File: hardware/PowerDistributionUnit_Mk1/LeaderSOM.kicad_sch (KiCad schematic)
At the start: 14 parts, among them J10 Logic Analyzer, J11 Logic Analyzer, J12 Logic Analyzer, U1 LeaderSOM

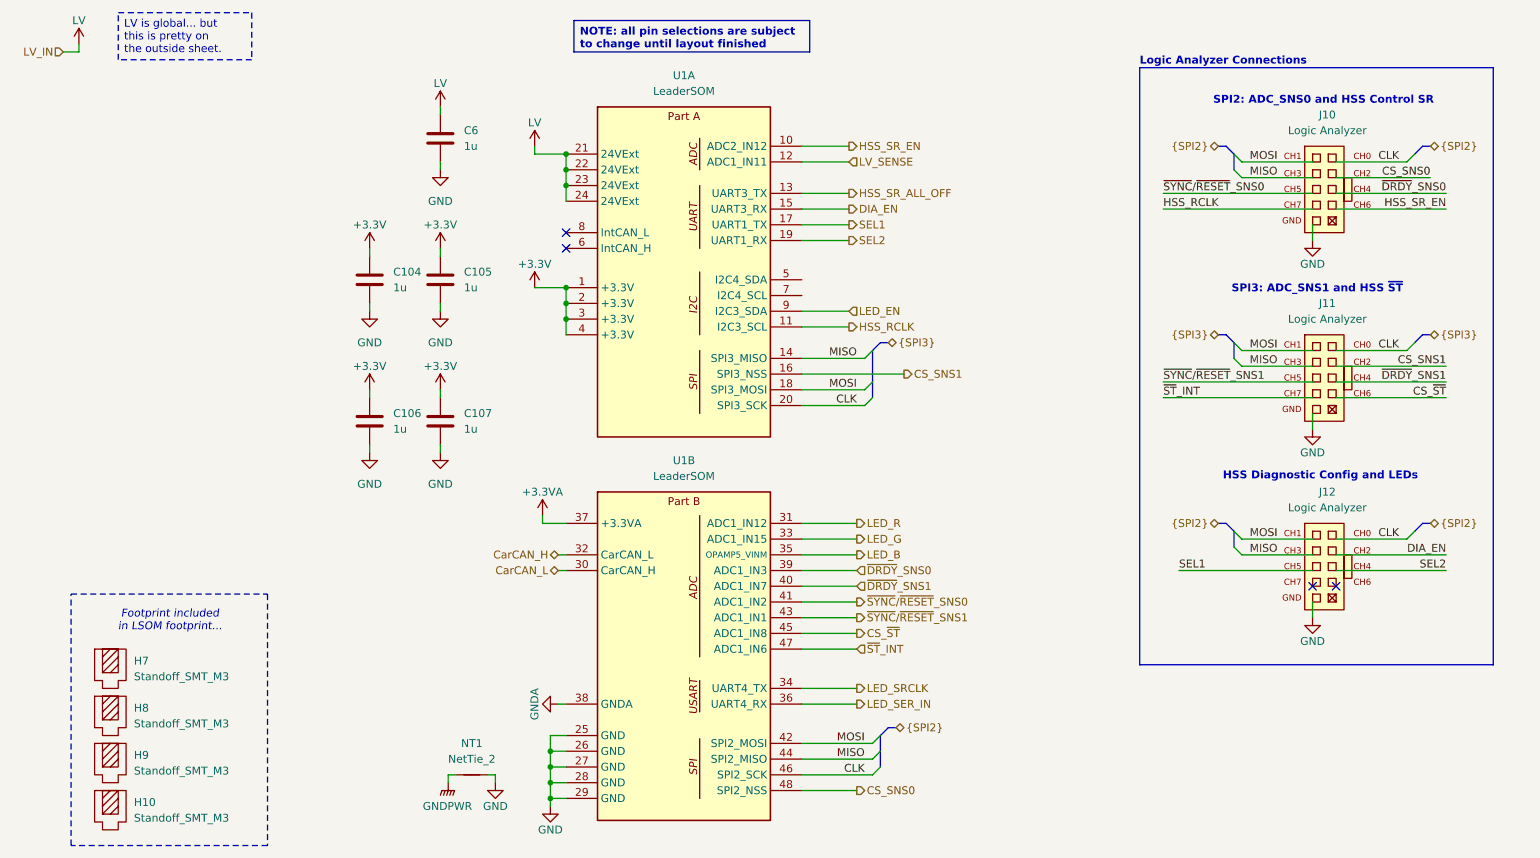
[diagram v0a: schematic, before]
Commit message: schematic updates (found switch, LED resistor values, LV sense ADC pin filter, removed unnecessary parallel resistors, switched to new SR), addressed review comments (input fuse, 3.3V LED, SPI naming fix)
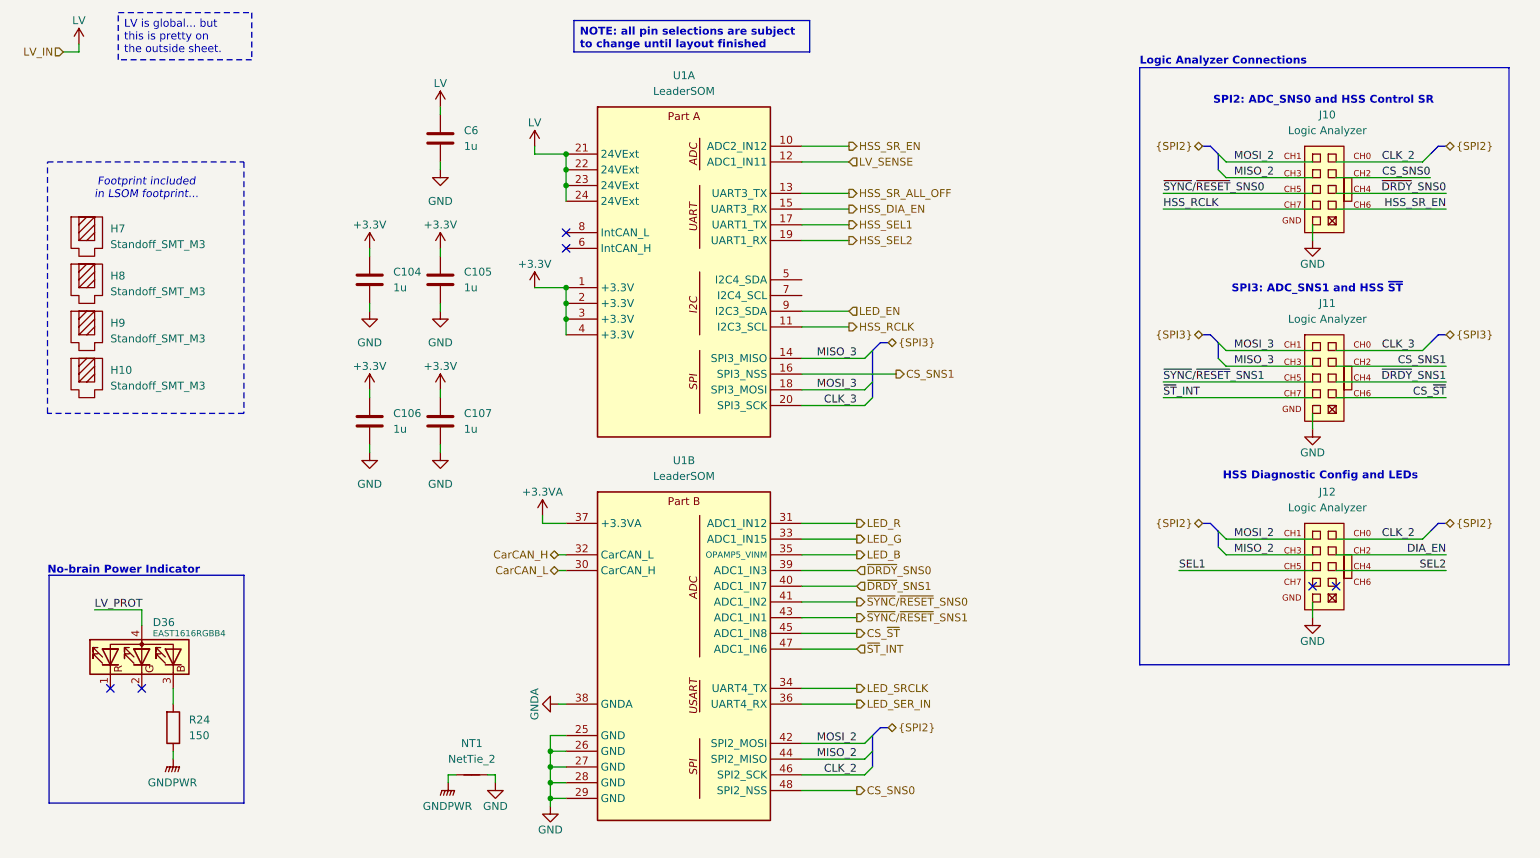
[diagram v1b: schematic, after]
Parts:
- added D36: EAST1616RGBB4, PowerDistributionUnitLib:Everlight_4-SMD, symbol PowerDistributionUnitLib:EAST1616RGBB4
- added R24: 150, Resistor_SMD:R_0603_1608Metric, symbol PowerDistributionUnitResistorLib:150
- U1: footprint PowerDistributionUnitLib:LeaderSOM_Standoff -> UTSVT_Special:LeaderSOM
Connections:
- net DIA_EN: no longer U1.15 (UART3_RX)
- net GNDPWR: now also R24.2
- net SEL1: no longer U1.17 (UART1_TX)
- net SEL2: no longer U1.19 (UART1_RX)
- net CLK renamed CLK_2
- net CLK_2: no longer J11.10 (CH0), U1.20 (SPI3_SCK)
- net MISO renamed MISO_2
- net MISO_2: no longer J11.7 (CH3), U1.14 (SPI3_MISO)
- net MOSI renamed MOSI_2
- net MOSI_2: no longer J11.9 (CH1), U1.18 (SPI3_MOSI)
- new net: D36.3 (BK), R24.1
- new net CLK_3: J11.10 (CH0), U1.20 (SPI3_SCK)
- new net HSS_DIA_EN: U1.15 (UART3_RX)
- new net HSS_SEL1: U1.17 (UART1_TX)
- new net HSS_SEL2: U1.19 (UART1_RX)
- new net LV_PROT: D36.4 (A)
- new net MISO_3: J11.7 (CH3), U1.14 (SPI3_MISO)
- new net MOSI_3: J11.9 (CH1), U1.18 (SPI3_MOSI)
- no-connect marks 4 -> 6
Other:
- note added: "No-brain Power Indicator"
- moved on the sheet: H10, H7, H8, H9

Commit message: fix LeaderSOM footprint, assign proper ADC crystal footprint
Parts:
- U1: footprint UTSVT_Special:LeaderSOM -> PowerDistributionUnitLib:LeaderSOM_Standoff
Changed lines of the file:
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@@
 			)
 		)
-		(property "Footprint" "UTSVT_Special:LeaderSOM"
+		(property "Footprint" "PowerDistributionUnitLib:LeaderSOM_Standoff"
 			(at 138.43 64.77 0)
 			(effects
@@
 			)
 		)
-		(property "Footprint" "UTSVT_Special:LeaderSOM"
+		(property "Footprint" "PowerDistributionUnitLib:LeaderSOM_Standoff"
 			(at 138.43 127 0)
 			(effects

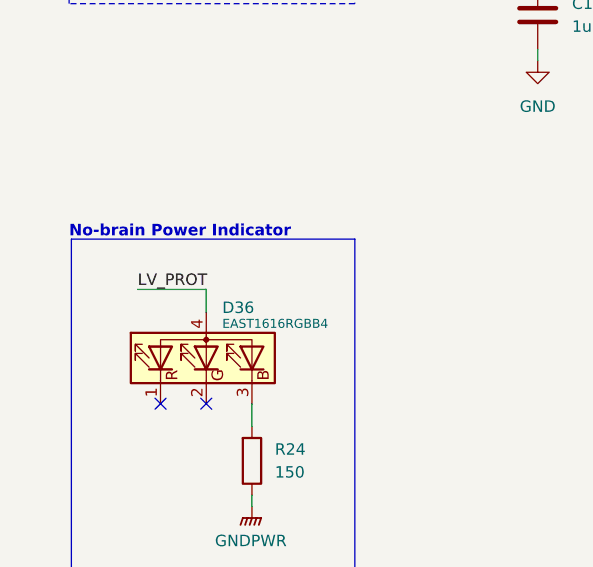
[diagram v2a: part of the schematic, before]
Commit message: started grouping/laying out non HSS components, fixed some schematic things (pins being connected to wrong adjacent thing, LEDs connected to wrong thing, etc.)
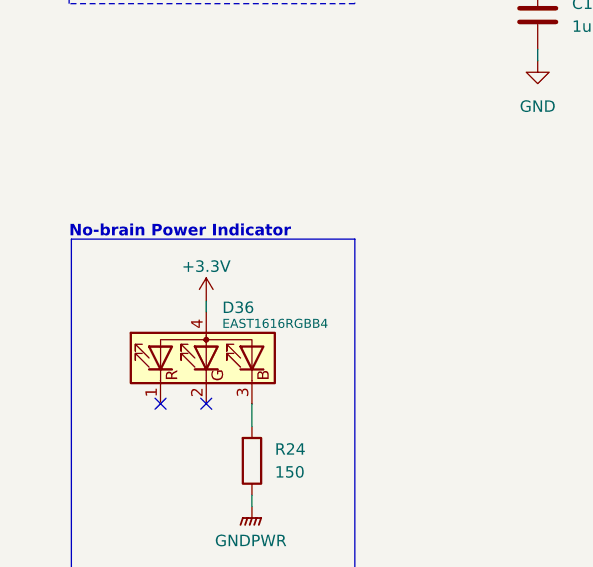
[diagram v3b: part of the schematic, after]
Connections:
- net LV_PROT is gone; now on net +3.3V: D36.4 (A)
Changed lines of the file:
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@@
-	(wire
-		(pts
-			(xy 50.8 119.38) (xy 50.8 121.92)
-		)
-		(stroke
-			(width 0)
-			(type default)
-		)
-	)
 	(wire
 		(pts
@@
 	(wire
 		(pts
-			(xy 43.18 119.38) (xy 50.8 119.38)
-		)
-		(stroke
-			(width 0)
-			(type default)
-		)
-	)
-	(wire
-		(pts
 			(xy 226.06 107.95) (xy 240.03 107.95)
 		)
@@
 		(pts
 			(xy 240.03 118.11) (xy 240.03 120.65)
+		)
+		(stroke
+			(width 0)
+			(type default)
+		)
+	)
+	(wire
+		(pts
+			(xy 50.8 120.65) (xy 50.8 121.92)
 		)
 		(stroke
@@
 			)
 			(justify right bottom)
-		)
-	)
-	(label "LV_PROT"
-		(at 43.18 119.38 0)
-		(effects
-			(font
-				(size 1.27 1.27)
-			)
-			(justify left bottom)
 		)
 	)
@@
 					(unit 1)
 				)
+			)
+		)
+	)
+	(symbol
+		(lib_id "power:+3.3V")
+		(at 50.8 120.65 0)
+		(mirror y)
+		(unit 1)
+		(exclude_from_sim no)
+		(in_bom yes)
+		(on_board yes)
+		(dnp no)
+		(property "Reference" "#PWR086"
+			(at 50.8 124.46 0)
+			(effects
+				(font
+					(size 1.27 1.27)
+				)
+				(hide yes)
+			)
+		)
+		(property "Value" "+3.3V"
+			(at 50.8 116.84 0)
+			(effects
+				(font
+					(size 1.27 1.27)
+				)
+			)
+		)
+		(property "Footprint" ""
+			(at 50.8 120.65 0)
+			(effects
+				(font
+					(size 1.27 1.27)
+				)
+				(hide yes)
+			)
+		)
+		(property "Datasheet" ""
+			(at 50.8 120.65 0)
+			(effects
+				(font
+					(size 1.27 1.27)
+				)
+				(hide yes)
+			)
+		)
+		(property "Description" "Power symbol creates a global label with name \"+3.3V\""
+			(at 50.8 120.65 0)
+			(effects
+				(font
+					(size 1.27 1.27)
+				)
+				(hide yes)
+			)
+		)
+		(pin "1"
+		)
+		(instances
+			(project "PowerDistributionUnit_Mk1"
+				(path "/6abaf095-8ba7-4306-8425-59a9eb37aa2b/9db45747-239d-4a98-a456-ca77cdc3d84b"
+					(reference "#PWR086")
+					(unit 1)
+				)

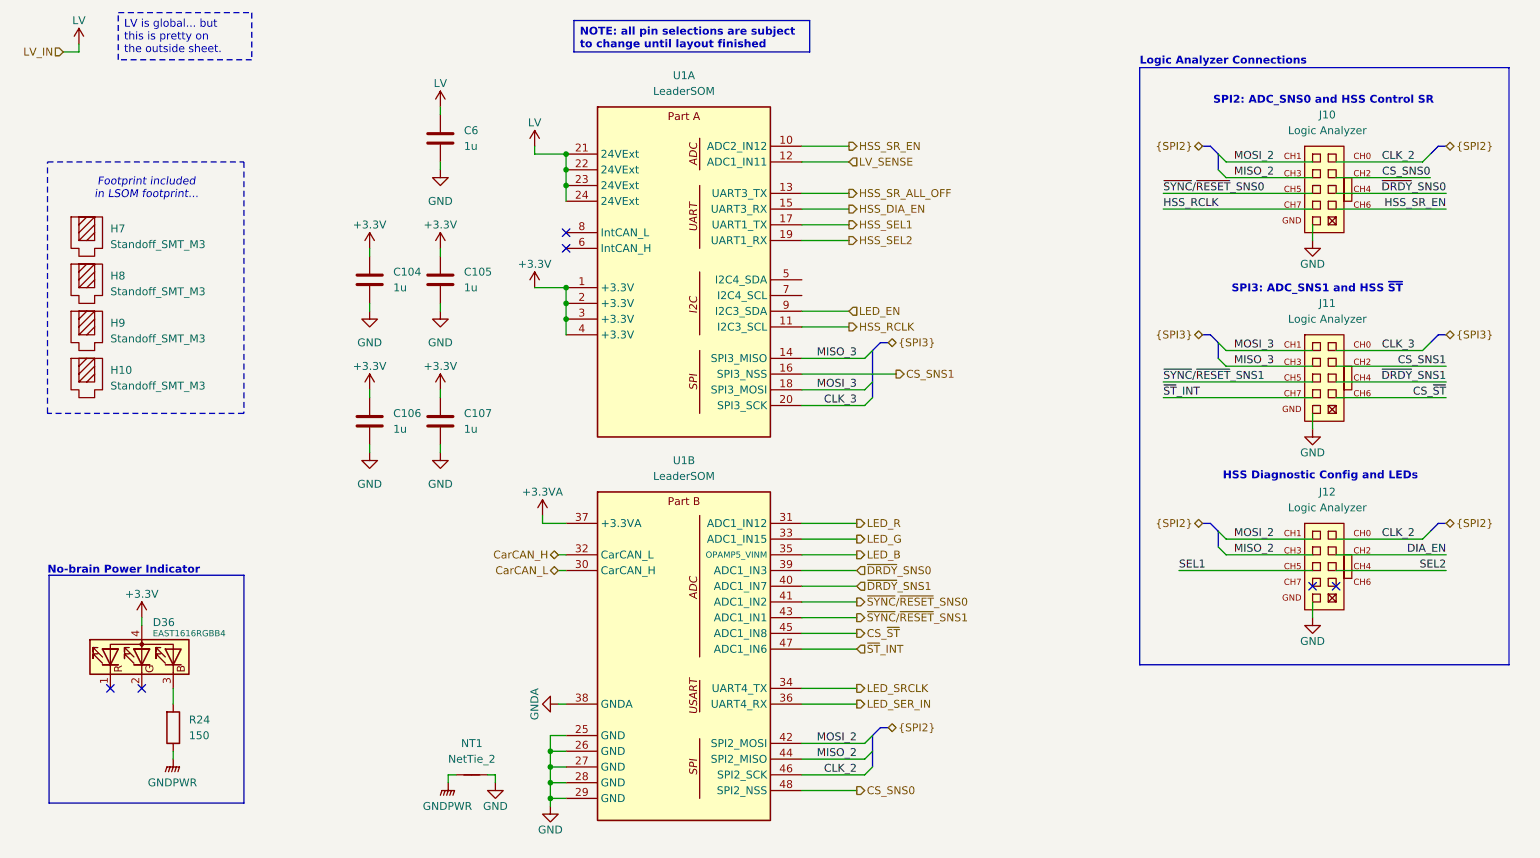
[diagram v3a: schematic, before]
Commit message: grouping of similar parts, zone fill adjustment, routing of ADCs under LSOM with GPIO connection adjustments, power input routing
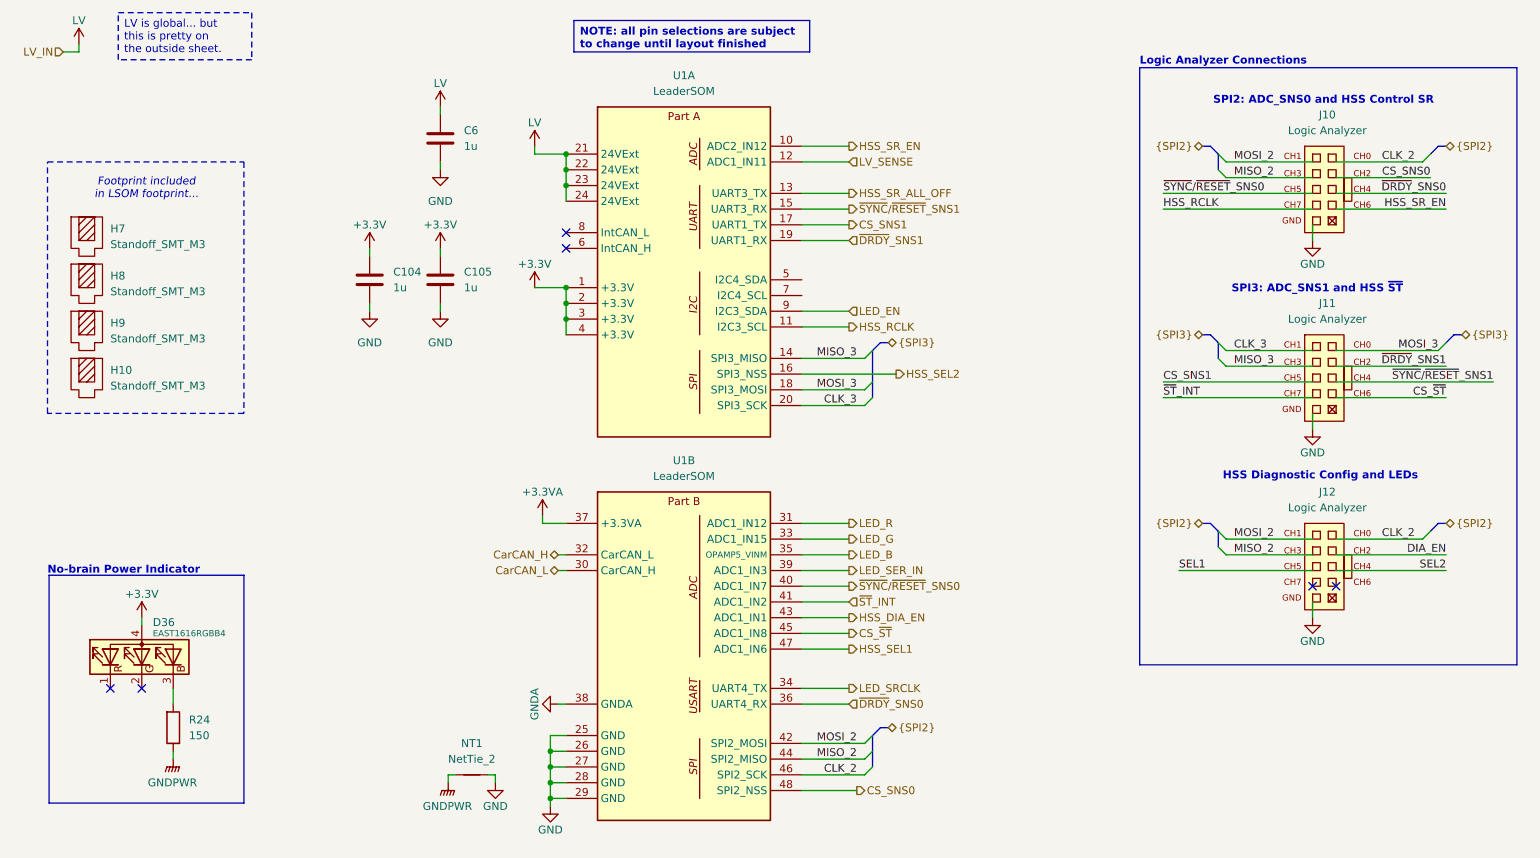
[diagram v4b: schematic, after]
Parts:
- removed C106, C107: 1u, Capacitor_SMD:C_0603_1608Metric, symbol PowerDistributionUnitCapacitorLib:1u
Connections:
- net CLK_3: now also J11.9 (CH1); no longer J11.10 (CH0)
- net CS_SNS1: now also J11.5 (CH5), U1.17 (UART1_TX); no longer J11.8 (CH2), U1.16 (SPI3_NSS)
- net HSS_DIA_EN: now also U1.43 (ADC1_IN1); no longer U1.15 (UART3_RX)
- net HSS_SEL1: now also U1.47 (ADC1_IN6); no longer U1.17 (UART1_TX)
- net HSS_SEL2: now also U1.16 (SPI3_NSS); no longer U1.19 (UART1_RX)
- net LED_SER_IN: now also U1.39 (ADC1_IN3); no longer U1.36 (UART4_RX)
- net MOSI_3: now also J11.10 (CH0); no longer J11.9 (CH1)
- net ~{DRDY}_SNS0: now also U1.36 (UART4_RX); no longer U1.39 (ADC1_IN3)
- net ~{DRDY}_SNS1: now also J11.8 (CH2), U1.19 (UART1_RX); no longer J11.6 (CH4), U1.40 (ADC1_IN7)
- net ~{ST}_INT: now also U1.41 (ADC1_IN2); no longer U1.47 (ADC1_IN6)
- net ~{SYNC}/~{RESET}_SNS0: now also U1.40 (ADC1_IN7); no longer U1.41 (ADC1_IN2)
- net ~{SYNC}/~{RESET}_SNS1: now also J11.6 (CH4), U1.15 (UART3_RX); no longer J11.5 (CH5), U1.43 (ADC1_IN1)
